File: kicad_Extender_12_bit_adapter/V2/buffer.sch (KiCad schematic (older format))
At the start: 8 parts, among them P1 Conn_02x06_Odd_Even, P2 Conn_01x04, P4 Conn_01x08_odd, P5 Conn_01x08_even, P6 Conn_01x01, P7 Conn_01x01

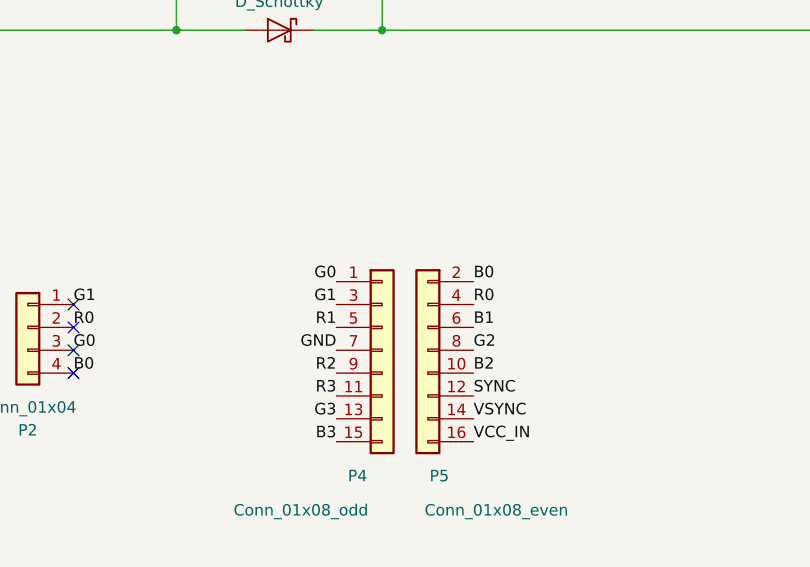
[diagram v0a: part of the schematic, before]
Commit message: Update 12 bit extender to V2
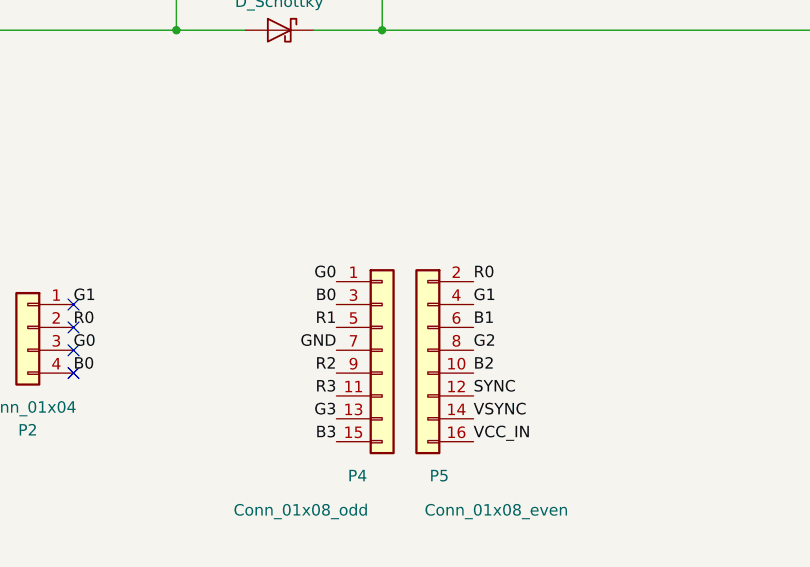
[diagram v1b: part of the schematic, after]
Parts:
- P1: footprint Connector_PinHeader_2.54mm:PinHeader_2x06_P2.54mm_Horizontal -> Connector_PinSocket_2.54mm:PinSocket_2x06_P2.54mm_Horizontal
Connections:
- net B0: now also P4.3 (Pin_3); no longer P5.2 (Pin_2)
- net G1: now also P5.4 (Pin_4); no longer P4.3 (Pin_3)
- net R0: now also P5.2 (Pin_2); no longer P5.4 (Pin_4)
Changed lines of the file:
@@
 F 0 "P1" H 9300 4217 50  0000 C CNN
 F 1 "Conn_02x06_Odd_Even" H 9300 4126 50  0000 C CNN
-F 2 "Connector_PinHeader_2.54mm:PinHeader_2x06_P2.54mm_Horizontal" H 9250 3800 50  0001 C CNN
+F 2 "Connector_PinSocket_2.54mm:PinSocket_2x06_P2.54mm_Horizontal" H 9250 3800 50  0001 C CNN
 F 3 "~" H 9250 3800 50  0001 C CNN
 	1    9250 3800
@@
 $EndComp
 Text Label 6100 2800 0    50   ~ 0
+G1
+Text Label 6100 2700 0    50   ~ 0
 R0
-Text Label 6100 2700 0    50   ~ 0
+Text Label 5500 2800 2    50   ~ 0
 B0
-Text Label 5500 2800 2    50   ~ 0
-G1
 Text Label 5500 2700 2    50   ~ 0
 G0
